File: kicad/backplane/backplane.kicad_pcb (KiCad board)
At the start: 2 copper layers, 120.6 x 92.7 mm, 4 parts, among them J1 DIN41612_02x32_AC, J2 DIN41612_02x32_AC, J3 DIN41612_02x32_AC, J4 DIN41612_02x32_AC

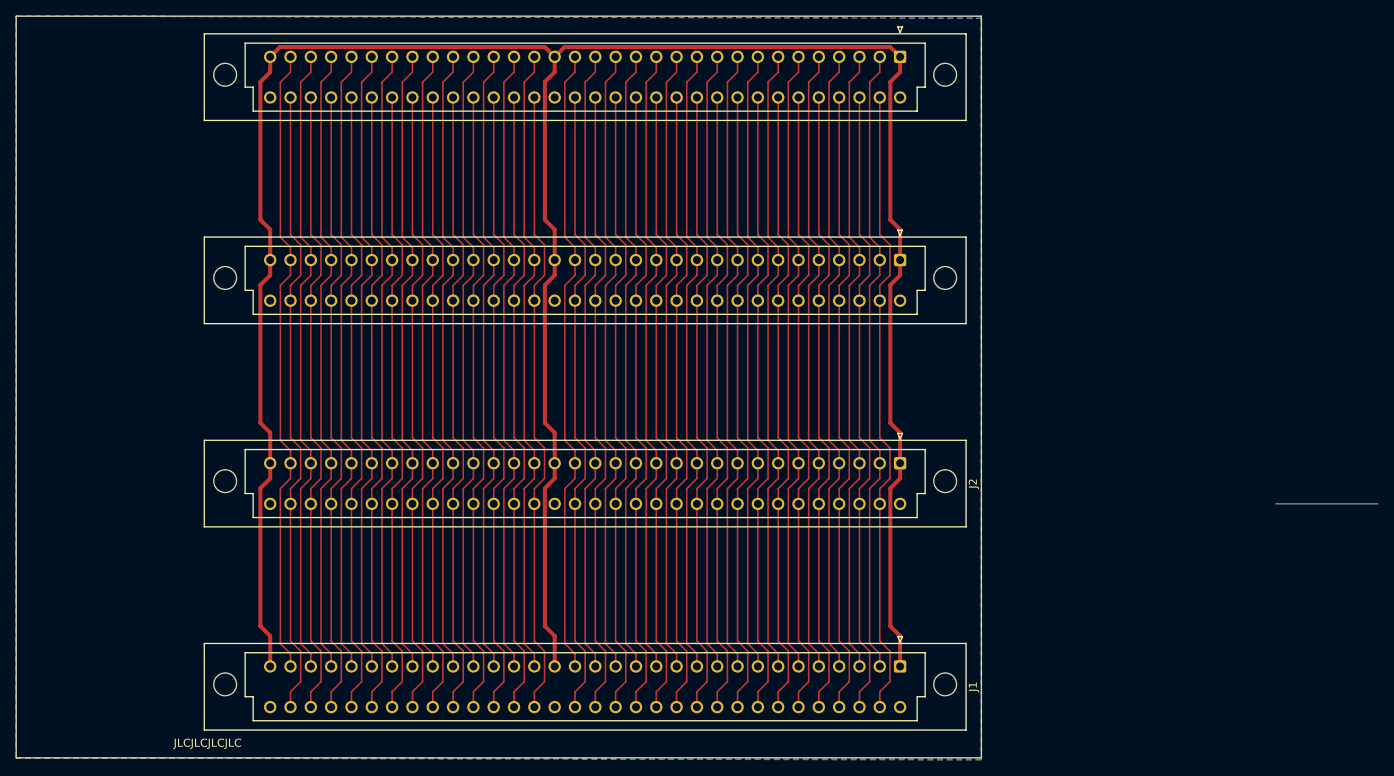
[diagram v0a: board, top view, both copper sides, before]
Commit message: cpu board & backplane as ordered
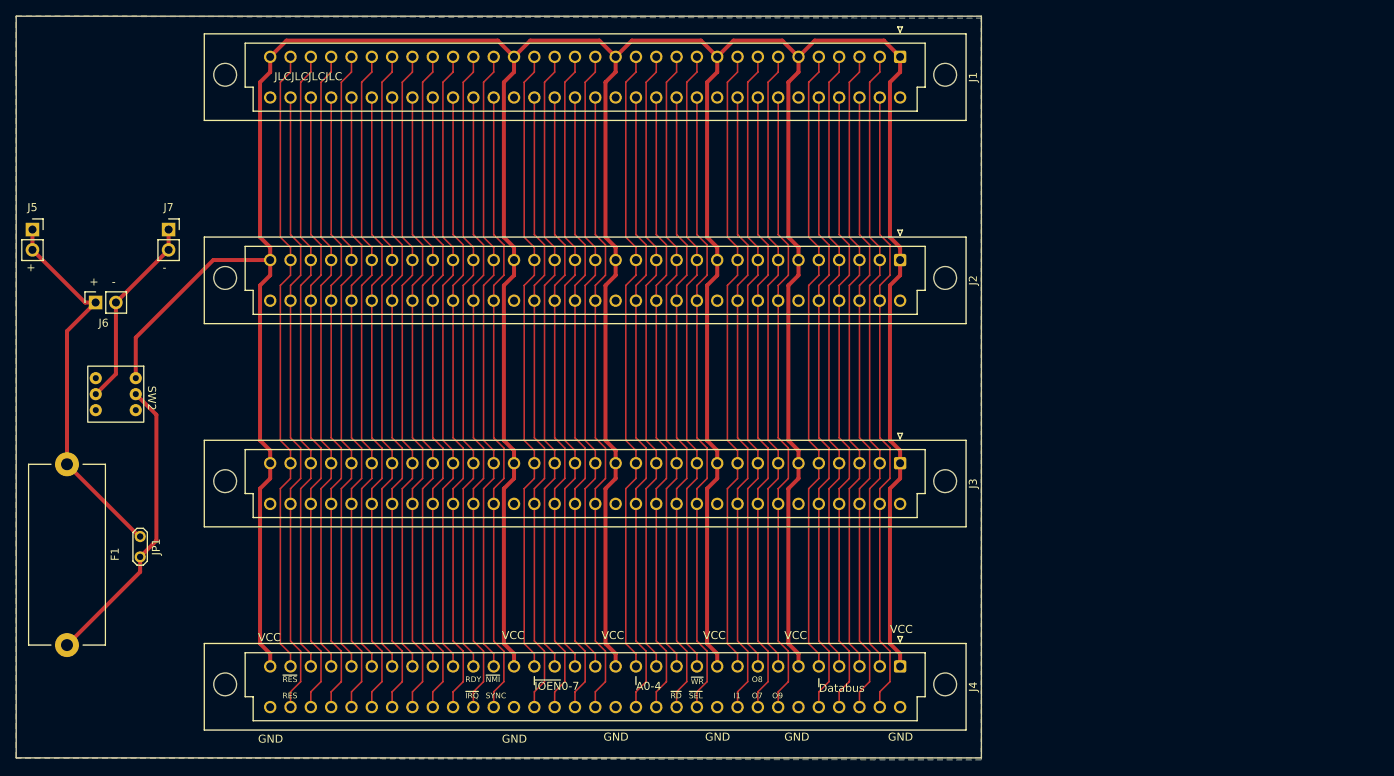
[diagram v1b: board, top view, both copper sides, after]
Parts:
- added F1: Fuse, Fuse:Fuseholder_Cylinder-5x20mm_Stelvio-Kontek_PTF78_Horizontal_Open, F.Cu at (29.2, 70.0)
- added J5: Conn_01x02_Socket, Connector_PinSocket_2.54mm:PinSocket_1x02_P2.54mm_Vertical, F.Cu at (24.9, 40.6)
- added J6: Conn_01x02_Socket, Connector_PinSocket_2.54mm:PinSocket_1x02_P2.54mm_Vertical, F.Cu at (32.8, 49.8)
- added J7: Conn_01x02_Socket, Connector_PinSocket_2.54mm:PinSocket_1x02_P2.54mm_Vertical, F.Cu at (41.9, 40.6)
- added JP1: Jumper_2_Open, TestPoint:TestPoint_2Pads_Pitch2.54mm_Drill0.8mm, F.Cu at (38.4, 79.0)
- added SW2: SW_PWR, sim82:7x7DPDT, F.Cu at (35.3, 61.2)
- moved J1 76.2 mm to (133.3, 19.1)
- moved J4 76.2 mm to (133.3, 95.2)
- moved J2 25.4 mm to (133.3, 44.5)
- moved J3 25.4 mm to (133.3, 69.8)
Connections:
- net /A10 renamed /CLOCK
- net /A12 renamed /DB0
- net /A13 renamed /DB2
- net /A14 renamed /DB4
- net /A15 renamed /DB6
- net /A3 renamed /AB0
- net /A4 renamed /AB2
- net /A5 renamed /AB4
- net /A6 renamed /~{IO_WR}
- net /D0 renamed /PLD_I1
- net /D1 renamed /PLD_O7
- net /D2 renamed /PLD_O9
- net /D4 renamed /DB1
- net /D5 renamed /DB3
- net /D6 renamed /DB5
- net /D7 renamed /DB7
- net /SYS_CLK renamed /RDY
- net /U11 renamed /~{IO_SEL_BUS}
- net /U12 renamed /~{IO_RD}
- net /U13 renamed /AB3
- net /U14 renamed /AB1
- net /U2 renamed /A26
- net /U21 renamed /SYNC
- net /U22 renamed /~{IRQ}
- net /U23 renamed /C23
- net /U24 renamed /C24
- net /U25 renamed /C25
- net /U26 renamed /C26
- net /U27 renamed /C27
- net /U28 renamed /C28
- net /U29 renamed /C29
- net /~{IO_SEL} renamed /A23
- net /~{SYS_CLK} renamed /~{NMI}
- J1 pad a10: /A7 -> VCC
- J1 pad a15: /A2 -> VCC
- J1 pad a16: /A1 -> /~{IOEN_06}
- J1 pad a17: /A0 -> /~{IOEN_04}
- J1 pad a18: VCC -> /~{IOEN_02_UART}
- J1 pad a19: /U0 -> /~{IOEN_00_GPIO0}
- J1 pad a20: /U1 -> VCC
- J1 pad a24: /~{IOEN_00_GPIO0} -> /A24
- J1 pad a25: /~{IOEN_01} -> /A25
- J1 pad a27: /~{IOEN_03} -> /A27
- J1 pad a28: /~{IOEN_04} -> /A28
- J1 pad a29: /~{IOEN_05} -> /A29
- J1 pad a30: /~{IOEN_06} -> /A30
- J1 pad a31: /~{IOEN_07} -> /~{RES}
- J1 pad a6: /A11 -> VCC
- J1 pad a8: /A9 -> /PLD_O8
- J1 pad a9: /A8 -> /A9
- J1 pad c10: /U10 -> GND
- J1 pad c15: /U15 -> GND
- J1 pad c16: /U16 -> /~{IOEN_07}
- J1 pad c17: /U17 -> /~{IOEN_05}
- J1 pad c18: GND -> /~{IOEN_03}
- J1 pad c19: /U19 -> /~{IOEN_01}
- J1 pad c20: /U20 -> GND
- J1 pad c30: /RES -> /C30
- J1 pad c31: /~{RES} -> /RES
- J1 pad c6: /D3 -> GND
- J2 pad a10: /A7 -> VCC
- J2 pad a15: /A2 -> VCC
- J2 pad a16: /A1 -> /~{IOEN_06}
- J2 pad a17: /A0 -> /~{IOEN_04}
- J2 pad a18: VCC -> /~{IOEN_02_UART}
- J2 pad a19: /U0 -> /~{IOEN_00_GPIO0}
- J2 pad a20: /U1 -> VCC
- J2 pad a24: /~{IOEN_00_GPIO0} -> /A24
- J2 pad a25: /~{IOEN_01} -> /A25
- J2 pad a27: /~{IOEN_03} -> /A27
- J2 pad a28: /~{IOEN_04} -> /A28
- J2 pad a29: /~{IOEN_05} -> /A29
- J2 pad a30: /~{IOEN_06} -> /A30
- J2 pad a31: /~{IOEN_07} -> /~{RES}
- J2 pad a6: /A11 -> VCC
- J2 pad a8: /A9 -> /PLD_O8
- J2 pad a9: /A8 -> /A9
- J2 pad c10: /U10 -> GND
- J2 pad c15: /U15 -> GND
- J2 pad c16: /U16 -> /~{IOEN_07}
- J2 pad c17: /U17 -> /~{IOEN_05}
- J2 pad c18: GND -> /~{IOEN_03}
- J2 pad c19: /U19 -> /~{IOEN_01}
- J2 pad c20: /U20 -> GND
- J2 pad c30: /RES -> /C30
- J2 pad c31: /~{RES} -> /RES
- J2 pad c6: /D3 -> GND
- J3 pad a10: /A7 -> VCC
- J3 pad a15: /A2 -> VCC
- J3 pad a16: /A1 -> /~{IOEN_06}
- J3 pad a17: /A0 -> /~{IOEN_04}
- J3 pad a18: VCC -> /~{IOEN_02_UART}
- J3 pad a19: /U0 -> /~{IOEN_00_GPIO0}
- J3 pad a20: /U1 -> VCC
- J3 pad a24: /~{IOEN_00_GPIO0} -> /A24
- J3 pad a25: /~{IOEN_01} -> /A25
- J3 pad a27: /~{IOEN_03} -> /A27
- J3 pad a28: /~{IOEN_04} -> /A28
- J3 pad a29: /~{IOEN_05} -> /A29
- J3 pad a30: /~{IOEN_06} -> /A30
- J3 pad a31: /~{IOEN_07} -> /~{RES}
- J3 pad a6: /A11 -> VCC
- J3 pad a8: /A9 -> /PLD_O8
- J3 pad a9: /A8 -> /A9
- J3 pad c10: /U10 -> GND
- J3 pad c15: /U15 -> GND
- J3 pad c16: /U16 -> /~{IOEN_07}
- J3 pad c17: /U17 -> /~{IOEN_05}
- J3 pad c18: GND -> /~{IOEN_03}
- J3 pad c19: /U19 -> /~{IOEN_01}
- J3 pad c20: /U20 -> GND
- J3 pad c30: /RES -> /C30
- J3 pad c31: /~{RES} -> /RES
- J3 pad c6: /D3 -> GND
- J4 pad a10: /A7 -> VCC
- J4 pad a15: /A2 -> VCC
- J4 pad a16: /A1 -> /~{IOEN_06}
- J4 pad a17: /A0 -> /~{IOEN_04}
- J4 pad a18: VCC -> /~{IOEN_02_UART}
- J4 pad a19: /U0 -> /~{IOEN_00_GPIO0}
- J4 pad a20: /U1 -> VCC
- J4 pad a24: /~{IOEN_00_GPIO0} -> /A24
- J4 pad a25: /~{IOEN_01} -> /A25
- J4 pad a27: /~{IOEN_03} -> /A27
- J4 pad a28: /~{IOEN_04} -> /A28
- J4 pad a29: /~{IOEN_05} -> /A29
- J4 pad a30: /~{IOEN_06} -> /A30
- J4 pad a31: /~{IOEN_07} -> /~{RES}
- J4 pad a6: /A11 -> VCC
- J4 pad a8: /A9 -> /PLD_O8
- J4 pad a9: /A8 -> /A9
- J4 pad c10: /U10 -> GND
- J4 pad c15: /U15 -> GND
- J4 pad c16: /U16 -> /~{IOEN_07}
- J4 pad c17: /U17 -> /~{IOEN_05}
- J4 pad c18: GND -> /~{IOEN_03}
- J4 pad c19: /U19 -> /~{IOEN_01}
- J4 pad c20: /U20 -> GND
- J4 pad c30: /RES -> /C30
- J4 pad c31: /~{RES} -> /RES
- J4 pad c6: /D3 -> GND
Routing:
- net VCC: track 331.2 -> 589.2 mm
- net /U19: track 79.4 -> 0.00 mm
- net /U17: track 79.4 -> 0.00 mm
- net /U1: track 79.4 -> 0.00 mm
- net /A2: track 79.4 -> 0.00 mm
- net /A11: track 79.4 -> 0.00 mm
- net /U10: track 79.4 -> 0.00 mm
- net /A24: track 0.00 -> 79.4 mm
- net /C30: track 0.00 -> 79.4 mm
- net /U16: track 79.4 -> 0.00 mm
- net /PLD_O8: track 0.00 -> 79.4 mm
- net /~{IOEN_02_UART}: track 0.00 -> 79.4 mm
- net /U20: track 79.4 -> 0.00 mm
- net /U15: track 79.4 -> 0.00 mm
- net /U0: track 79.4 -> 0.00 mm
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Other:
- board text added: "+"
- board text added: "-"
- board text added: "A0-4"
- board text added: "Databus"
- board text added: "GND"
- board text added: "I1"
- board text added: "O7"
- board text added: "O8"
- board text added: "O9"
- board text added: "RDY"
- board text added: "RES"
- board text added: "SYNC"
- board text added: "VCC"
- board text added: "~{IOEN}0-7"
- board text added: "~{IRQ}"
- board text added: "~{NMI}"
- board text added: "~{RD}"
- board text added: "~{RES}"
- board text added: "~{SEL}"
- board text added: "~{WR}"
